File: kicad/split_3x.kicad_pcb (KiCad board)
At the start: 2 copper layers, 127.3 x 121.2 mm, 87 parts, among them SW1 SW_Push, SW2 SW_Push, SW3 Rotary_Encoder_Switch, SW4 Rotary_Encoder_Switch, SW5 SW_DIP_x01, SW6 SW_DIP_x01, U1 ProMicro, U2 TRRS

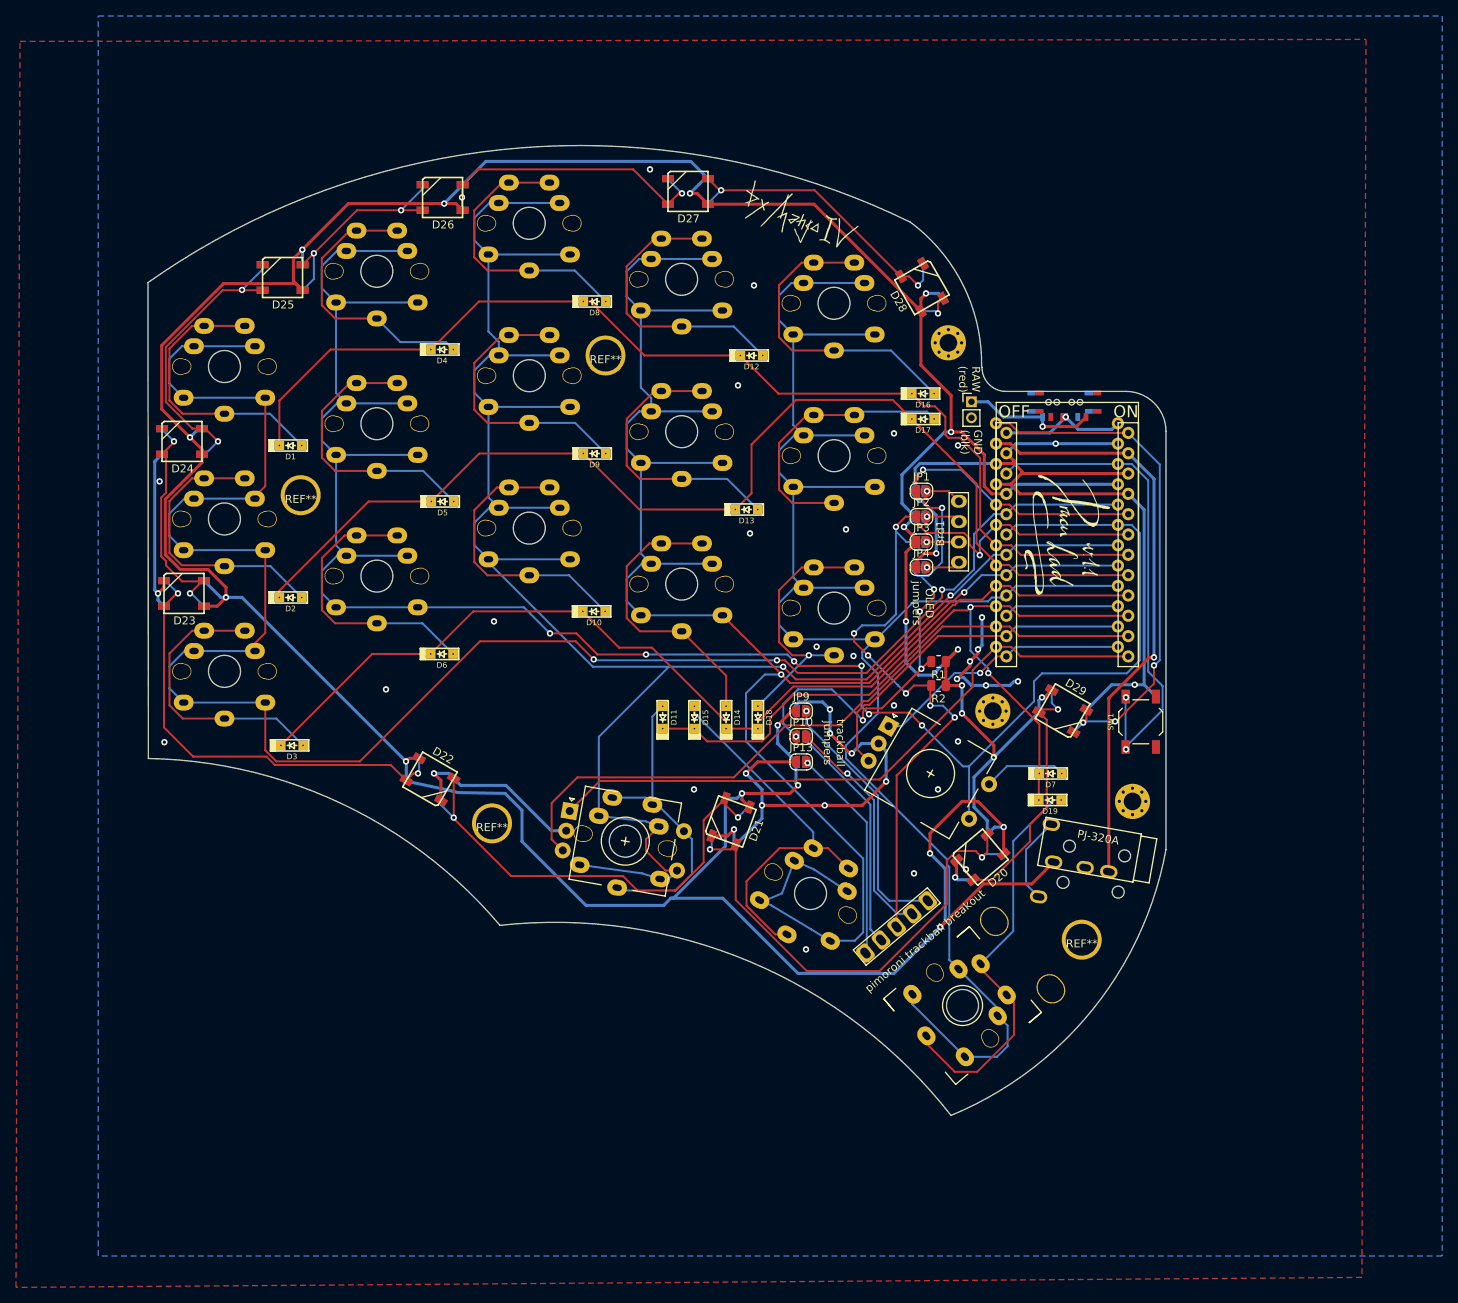
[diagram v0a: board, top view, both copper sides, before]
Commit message: added millmax hotswappable sockets
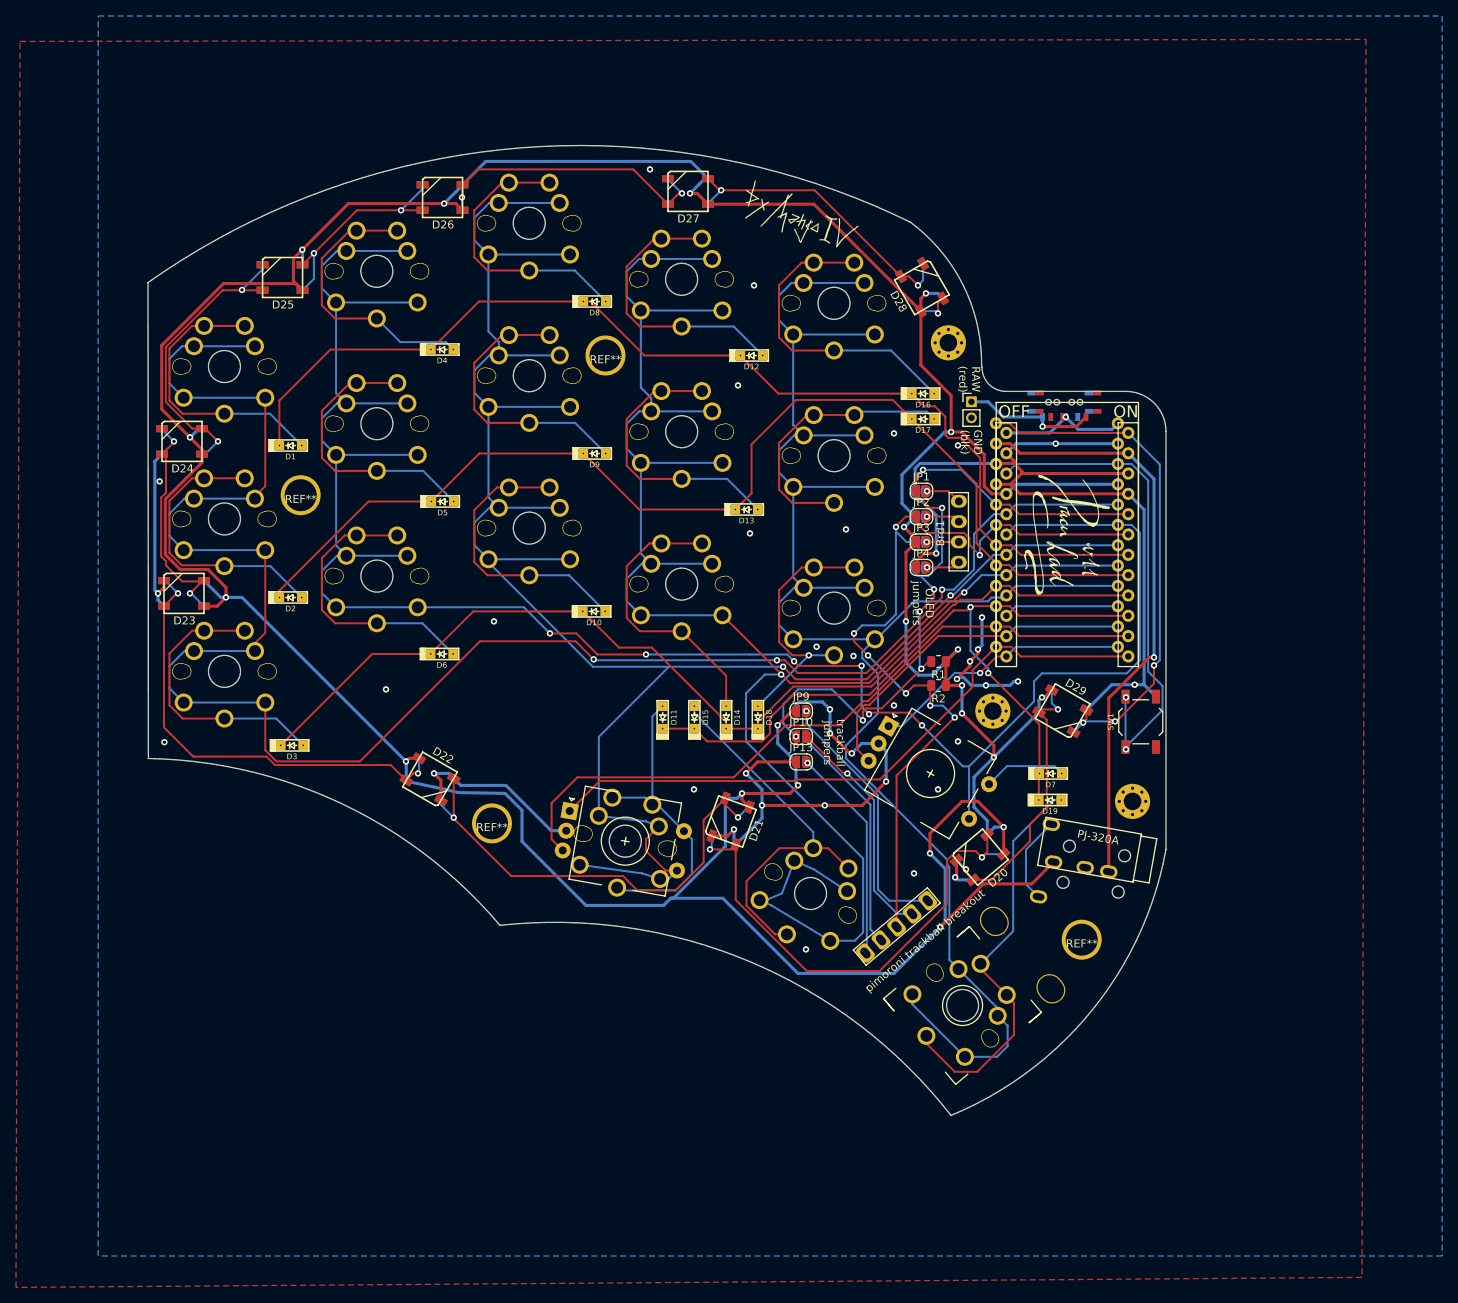
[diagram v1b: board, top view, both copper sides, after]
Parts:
- MX1, MX10, MX11, MX12, MX13, MX14, MX15, MX16, MX17, MX18, MX2, MX3, MX4, MX5, MX6, MX7, MX8, MX9: footprint other_parts:CherryMX_Choc_1u_reversible -> other_parts:MillMax_CherryMX_Choc_1u_reversible
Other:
- net class Default removed
- net class Power removed
- net class TRRSData removed
